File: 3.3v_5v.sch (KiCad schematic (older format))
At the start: 15 parts, among them J1 Jack-DC, SW1 SW_Push_SPDT, U1 AP1117-33

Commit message: duży update, gotowe pcb
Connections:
- net labels added: GNDA
- wire segments 27 -> 30
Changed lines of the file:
@@
 EESchema Schematic File Version 4
+LIBS:WELLER-cache
 EELAYER 29 0
 EELAYER END
@@
 $EndComp
 Wire Wire Line
-	3300 2650 3600 2650
+	3300 2650 3450 2650
 $Comp
 L power:GND #PWR0106
@@
 $EndComp
 Wire Wire Line
-	4000 3600 4000 2950
+	4000 3600 4000 3100
 Wire Wire Line
 	3600 2950 3600 3600
@@
 Wire Wire Line
 	2000 2550 2200 2550
+$Comp
+L power:PWR_FLAG #FLG0102
+U 1 1 5CF25261
+P 3450 2650
+F 0 "#FLG0102" H 3450 2725 50  0001 C CNN
+F 1 "PWR_FLAG" H 3450 2823 50  0000 C CNN
+F 2 "" H 3450 2650 50  0001 C CNN
+F 3 "~" H 3450 2650 50  0001 C CNN
+	1    3450 2650
+	1    0    0    -1
+$EndComp
+Connection ~ 3450 2650
+Wire Wire Line
+	3450 2650 3600 2650
+$Comp
+L power:PWR_FLAG #FLG0103
+U 1 1 5CF256F8
+P 4000 3100
+F 0 "#FLG0103" H 4000 3175 50  0001 C CNN
+F 1 "PWR_FLAG" V 4000 3228 50  0000 L CNN
+F 2 "" H 4000 3100 50  0001 C CNN
+F 3 "~" H 4000 3100 50  0001 C CNN
+	1    4000 3100
+	0    1    1    0
+$EndComp
+Connection ~ 4000 3100
+Wire Wire Line
+	4000 3100 4000 2950
+$Comp
+L power:GND #PWR0136
+U 1 1 5CEE3547
+P 4600 4350
+F 0 "#PWR0136" H 4600 4100 50  0001 C CNN
+F 1 "GND" H 4605 4177 50  0000 C CNN
+F 2 "" H 4600 4350 50  0001 C CNN
+F 3 "" H 4600 4350 50  0001 C CNN
+	1    4600 4350
+	1    0    0    -1
+$EndComp
+$Comp
+L power:GNDA #PWR0140
+U 1 1 5CEE3C79
+P 4850 4350
+F 0 "#PWR0140" H 4850 4100 50  0001 C CNN
+F 1 "GNDA" H 4855 4177 50  0000 C CNN
+F 2 "" H 4850 4350 50  0001 C CNN
+F 3 "" H 4850 4350 50  0001 C CNN
+	1    4850 4350
+	1    0    0    -1
+$EndComp
+Wire Wire Line
+	4600 4350 4850 4350
 $EndSCHEMATC

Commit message: duży update, drc przechodzi
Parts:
- removed H1, H2, H3, H4: MountingHole, MountingHole:MountingHole_2.2mm_M2, symbol Mechanical:MountingHole
- J1: footprint Connector_BarrelJack:BarrelJack_Horizontal -> symbols:jackDC_cutout
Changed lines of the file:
@@
 EESchema Schematic File Version 4
 LIBS:WELLER-cache
-EELAYER 26 0
+EELAYER 29 0
 EELAYER END
 $Descr A4 11693 8268
@@
 F 0 "J1" H 1057 3075 50  0000 C CNN
 F 1 "Jack-DC" H 1057 2984 50  0000 C CNN
-F 2 "Connector_BarrelJack:BarrelJack_Horizontal" H 1050 2710 50  0001 C CNN
+F 2 "symbols:jackDC_cutout" H 1050 2710 50  0001 C CNN
 F 3 "~" H 1050 2710 50  0001 C CNN
 	1    1000 2750
@@
 	2200 2550 2200 2650
 Connection ~ 2200 2650
-$Comp
-L Mechanical:MountingHole H1
-U 1 1 5CC1244A
-P 2950 1200
-F 0 "H1" H 3050 1246 50  0000 L CNN
-F 1 "MountingHole" H 3050 1155 50  0000 L CNN
-F 2 "MountingHole:MountingHole_2.2mm_M2" H 2950 1200 50  0001 C CNN
-F 3 "~" H 2950 1200 50  0001 C CNN
-	1    2950 1200
-	1    0    0    -1
-$EndComp
-$Comp
-L Mechanical:MountingHole H2
-U 1 1 5CC12623
-P 2950 1400
-F 0 "H2" H 3050 1446 50  0000 L CNN
-F 1 "MountingHole" H 3050 1355 50  0000 L CNN
-F 2 "MountingHole:MountingHole_2.2mm_M2" H 2950 1400 50  0001 C CNN
-F 3 "~" H 2950 1400 50  0001 C CNN
-	1    2950 1400
-	1    0    0    -1
-$EndComp
-$Comp
-L Mechanical:MountingHole H3
-U 1 1 5CC127F9
-P 2950 1600
-F 0 "H3" H 3050 1646 50  0000 L CNN
-F 1 "MountingHole" H 3050 1555 50  0000 L CNN
-F 2 "MountingHole:MountingHole_2.2mm_M2" H 2950 1600 50  0001 C CNN
-F 3 "~" H 2950 1600 50  0001 C CNN
-	1    2950 1600
-	1    0    0    -1
-$EndComp
-$Comp
-L Mechanical:MountingHole H4
-U 1 1 5CC129B7
-P 2950 1800
-F 0 "H4" H 3050 1846 50  0000 L CNN
-F 1 "MountingHole" H 3050 1755 50  0000 L CNN
-F 2 "MountingHole:MountingHole_2.2mm_M2" H 2950 1800 50  0001 C CNN
-F 3 "~" H 2950 1800 50  0001 C CNN
-	1    2950 1800
-	1    0    0    -1
-$EndComp
 Wire Wire Line
 	1550 2450 1550 2350

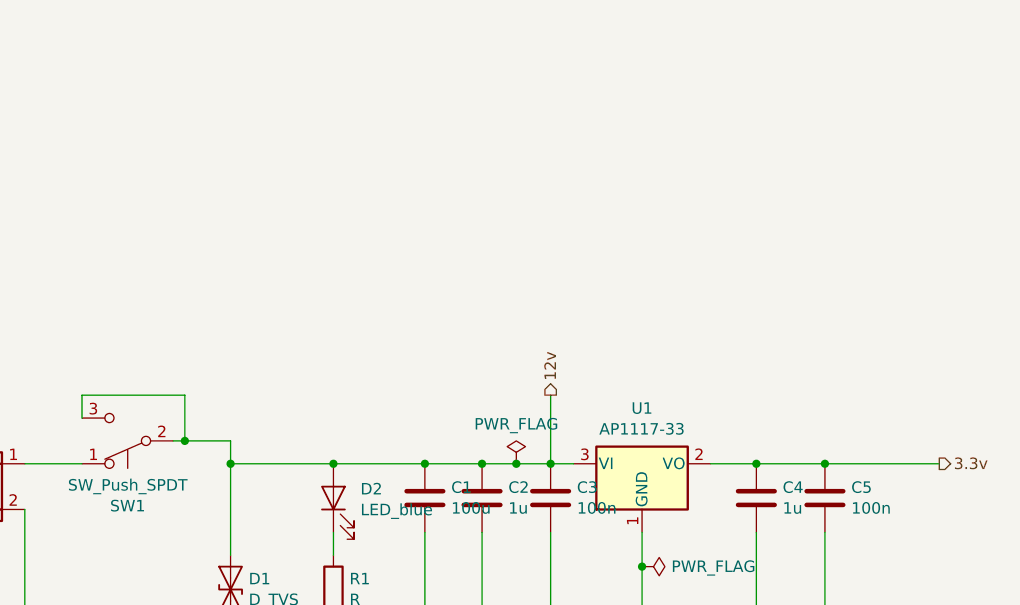
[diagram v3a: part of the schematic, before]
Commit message: dodanie pomiaru napięcia zasilającego grzałkę
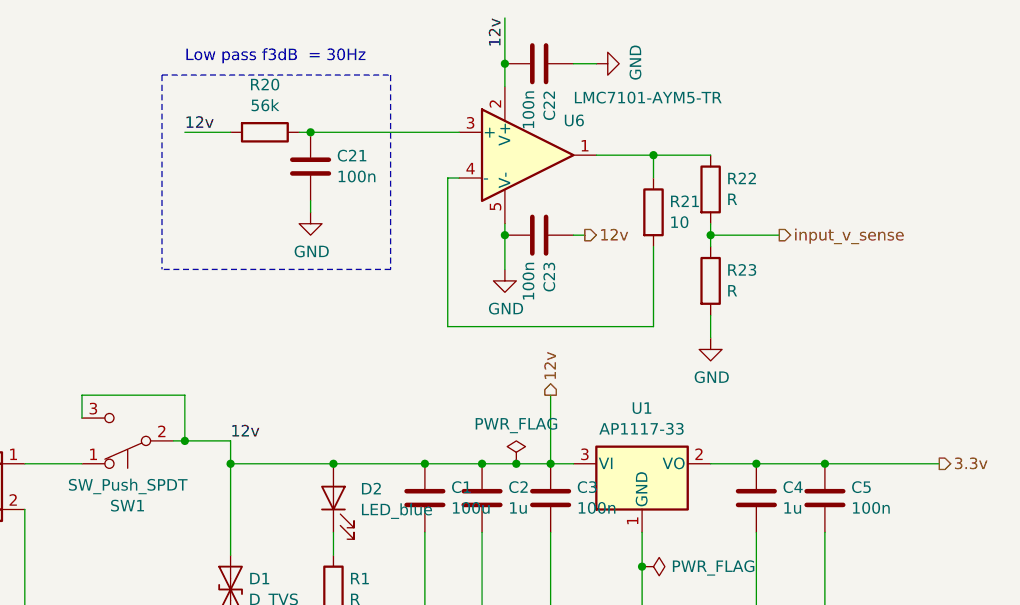
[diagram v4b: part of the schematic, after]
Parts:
- added C21, C22, C23: 100n, Capacitor_SMD:C_0603_1608Metric_Pad1.05x0.95mm_HandSolder, symbol Device:C
- added R20: 56k, Resistor_SMD:R_0603_1608Metric_Pad1.05x0.95mm_HandSolder, symbol Device:R
- added R21: 10, Resistor_SMD:R_0603_1608Metric_Pad1.05x0.95mm_HandSolder, symbol Device:R
- added R22, R23: R, Resistor_SMD:R_0603_1608Metric_Pad1.05x0.95mm_HandSolder, symbol Device:R
- added U6: LMC7101-AYM5-TR, Package_TO_SOT_SMD:SOT-23-5, symbol russian-nixies:LMC7101-AYM5-TR
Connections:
- net 12v: now also C22.2, C23.1, R20.2, U6.2 (V+)
- net GND: now also C21.2, C22.1, C23.2, R23.2, U6.5 (V-)
- new net: R21.1, R22.1, U6.1
- new net: C21.1, R20.1, U6.3 (+)
- new net: R21.2, U6.4 (-)
- new net input_v_sense: R22.2, R23.1
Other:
- note added: "Low pass f3dB = 30Hz"
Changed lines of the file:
@@
 Wire Wire Line
 	4600 4350 4850 4350
+$Comp
+L russian-nixies:LMC7101-AYM5-TR U6
+U 1 1 5D06EFCA
+P 3500 1300
+F 0 "U6" H 3750 1450 50  0000 R CNN
+F 1 "LMC7101-AYM5-TR" H 4350 1550 50  0000 R CNN
+F 2 "Package_TO_SOT_SMD:SOT-23-5" H 3400 1100 50  0001 L CNN
+F 3 "http://ww1.microchip.com/downloads/en/DeviceDoc/22141b.pdf" H 3500 1500 50  0001 C CNN
+	1    3500 1300
+	1    0    0    -1
+$EndComp
+$Comp
+L power:GND #PWR0132
+U 1 1 5D072379
+P 3400 1800
+F 0 "#PWR0132" H 3400 1550 50  0001 C CNN
+F 1 "GND" H 3405 1627 50  0000 C CNN
+F 2 "" H 3400 1800 50  0001 C CNN
+F 3 "" H 3400 1800 50  0001 C CNN
+	1    3400 1800
+	1    0    0    -1
+$EndComp
+$Comp
+L Device:C C23
+U 1 1 5D072847
+P 3550 1650
+F 0 "C23" H 3665 1696 50  0000 L CNN
+F 1 "100n" H 3665 1605 50  0000 L CNN
+F 2 "Capacitor_SMD:C_0603_1608Metric_Pad1.05x0.95mm_HandSolder" H 3588 1500 50  0001 C CNN
+F 3 "~" H 3550 1650 50  0001 C CNN
+	1    3550 1650
+	0    1    1    0
+$EndComp
+$Comp
+L Device:C C22
+U 1 1 5D072EC9
+P 3550 900
+F 0 "C22" H 3665 946 50  0000 L CNN
+F 1 "100n" H 3665 855 50  0000 L CNN
+F 2 "Capacitor_SMD:C_0603_1608Metric_Pad1.05x0.95mm_HandSolder" H 3588 750 50  0001 C CNN
+F 3 "~" H 3550 900 50  0001 C CNN
+	1    3550 900
+	0    1    1    0
+$EndComp
+Wire Wire Line
+	3400 1000 3400 900
+Connection ~ 3400 900
+Wire Wire Line
+	3400 900  3400 700
+Wire Wire Line
+	3400 1600 3400 1650
+Connection ~ 3400 1650
+Wire Wire Line
+	3400 1650 3400 1800
+$Comp
+L power:GND #PWR0133
+U 1 1 5D076440
+P 3800 900
+F 0 "#PWR0133" H 3800 650 50  0001 C CNN
+F 1 "GND" H 3805 727 50  0000 C CNN
+F 2 "" H 3800 900 50  0001 C CNN
+F 3 "" H 3800 900 50  0001 C CNN
+	1    3800 900
+	0    -1   -1   0
+$EndComp
+Wire Wire Line
+	3800 900  3700 900
+Text HLabel 3750 1650 2    50   Output ~ 0
+12v
+Wire Wire Line
+	3750 1650 3700 1650
+Wire Wire Line
+	3800 1300 4050 1300
+Text HLabel 4600 1650 2    50   Output ~ 0
+input_v_sense
+Wire Wire Line
+	3150 1400 3150 2050
+Wire Wire Line
+	3150 2050 4050 2050
+Wire Wire Line
+	4050 2050 4050 1700
+Wire Wire Line
+	3150 1400 3200 1400
+$Comp
+L Device:R R21
+U 1 1 5D079D81
+P 4050 1550
+F 0 "R21" H 4120 1596 50  0000 L CNN
+F 1 "10" H 4120 1505 50  0000 L CNN
+F 2 "Resistor_SMD:R_0603_1608Metric_Pad1.05x0.95mm_HandSolder" V 3980 1550 50  0001 C CNN
+F 3 "~" H 4050 1550 50  0001 C CNN
+	1    4050 1550
+	1    0    0    -1
+$EndComp
+Wire Wire Line
+	4050 1300 4050 1400
+Connection ~ 4050 1300
+Wire Wire Line
+	4050 1300 4300 1300
+$Comp
+L Device:R R20
+U 1 1 5D07C6AC
+P 2350 1200
+F 0 "R20" V 2143 1200 50  0000 C CNN
+F 1 "56k" V 2234 1200 50  0000 C CNN
+F 2 "Resistor_SMD:R_0603_1608Metric_Pad1.05x0.95mm_HandSolder" V 2280 1200 50  0001 C CNN
+F 3 "~" H 2350 1200 50  0001 C CNN
+	1    2350 1200
+	0    1    1    0
+$EndComp
+$Comp
+L Device:C C21
+U 1 1 5D07CF1C
+P 2550 1350
+F 0 "C21" H 2665 1396 50  0000 L CNN
+F 1 "100n" H 2665 1305 50  0000 L CNN
+F 2 "Capacitor_SMD:C_0603_1608Metric_Pad1.05x0.95mm_HandSolder" H 2588 1200 50  0001 C CNN
+F 3 "~" H 2550 1350 50  0001 C CNN
+	1    2550 1350
+	1    0    0    -1
+$EndComp
+$Comp
+L power:GND #PWR0135
+U 1 1 5D07D74D
+P 2550 1550
+F 0 "#PWR0135" H 2550 1300 50  0001 C CNN
+F 1 "GND" H 2555 1377 50  0000 C CNN
+F 2 "" H 2550 1550 50  0001 C CNN
+F 3 "" H 2550 1550 50  0001 C CNN
+	1    2550 1550
+	1    0    0    -1
+$EndComp
+Wire Wire Line
+	2550 1550 2550 1500
+Wire Wire Line
+	2500 1200 2550 1200
+Connection ~ 2550 1200
+Wire Wire Line
+	2550 1200 3200 1200
+Wire Wire Line
+	2000 1200 2200 1200
+Text Label 2200 2550 0    50   ~ 0
+12v
+Text Label 2000 1200 0    50   ~ 0
+12v
+Text Label 3400 700  3    50   ~ 0
+12v
+Text Notes 2000 900  0    50   ~ 0
+Low pass f3dB  = 30Hz
+Wire Notes Line
+	1900 950  2900 950
+Wire Notes Line
+	2900 1800 1900 1800
+Wire Notes Line
+	1900 950  1900 1800
+Wire Notes Line
+	2900 950  2900 1800
+$Comp
+L Device:R R22
+U 1 1 5D0A0AC8
+P 4300 1450
+F 0 "R22" H 4370 1496 50  0000 L CNN
+F 1 "R" H 4370 1405 50  0000 L CNN
+F 2 "Resistor_SMD:R_0603_1608Metric_Pad1.05x0.95mm_HandSolder" V 4230 1450 50  0001 C CNN
+F 3 "~" H 4300 1450 50  0001 C CNN
+	1    4300 1450
+	1    0    0    -1
+$EndComp
+$Comp
+L Device:R R23
+U 1 1 5D0A0DAA
+P 4300 1850
+F 0 "R23" H 4370 1896 50  0000 L CNN
+F 1 "R" H 4370 1805 50  0000 L CNN
+F 2 "Resistor_SMD:R_0603_1608Metric_Pad1.05x0.95mm_HandSolder" V 4230 1850 50  0001 C CNN
+F 3 "~" H 4300 1850 50  0001 C CNN
+	1    4300 1850
+	1    0    0    -1
+$EndComp
+$Comp
+L power:GND #PWR0141
+U 1 1 5D0A0FB3
+P 4300 2100
+F 0 "#PWR0141" H 4300 1850 50  0001 C CNN
+F 1 "GND" H 4305 1927 50  0000 C CNN
+F 2 "" H 4300 2100 50  0001 C CNN
+F 3 "" H 4300 2100 50  0001 C CNN
+	1    4300 2100
+	1    0    0    -1
+$EndComp
+Wire Wire Line
+	4300 2000 4300 2100
+Wire Wire Line
+	4300 1600 4300 1650
+Wire Wire Line
+	4600 1650 4300 1650
+Connection ~ 4300 1650
+Wire Wire Line
+	4300 1650 4300 1700
 $EndSCHEMATC

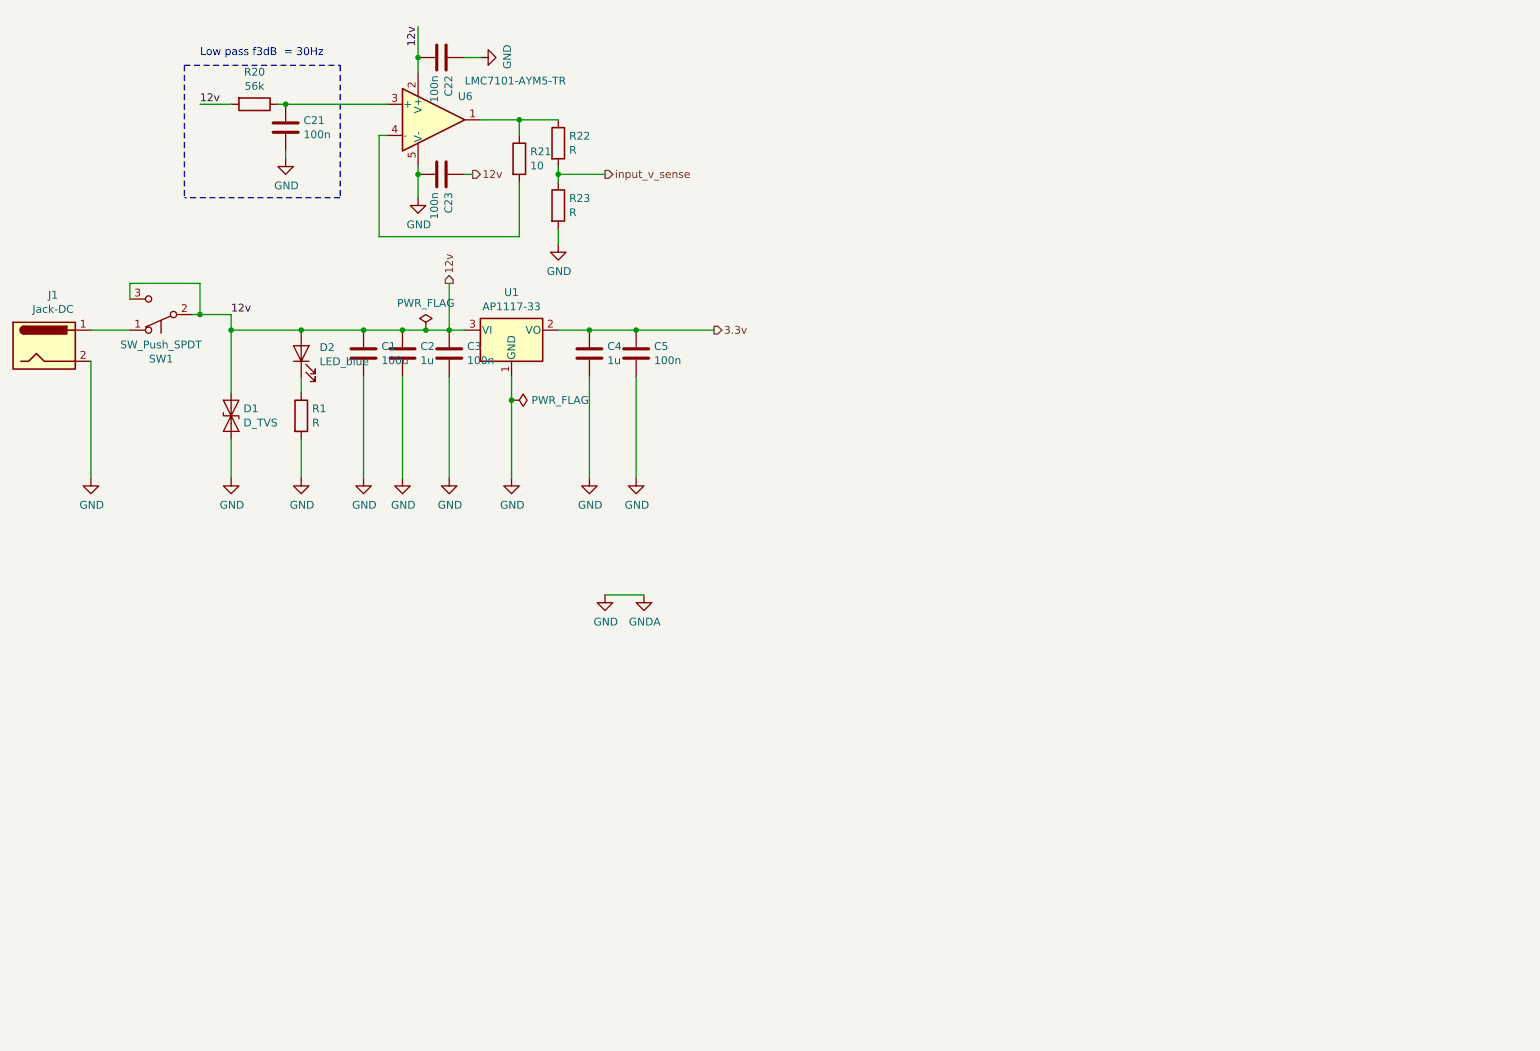
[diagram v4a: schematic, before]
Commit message: poprawki głownie na pcb zaokrąglenie strony z grotem
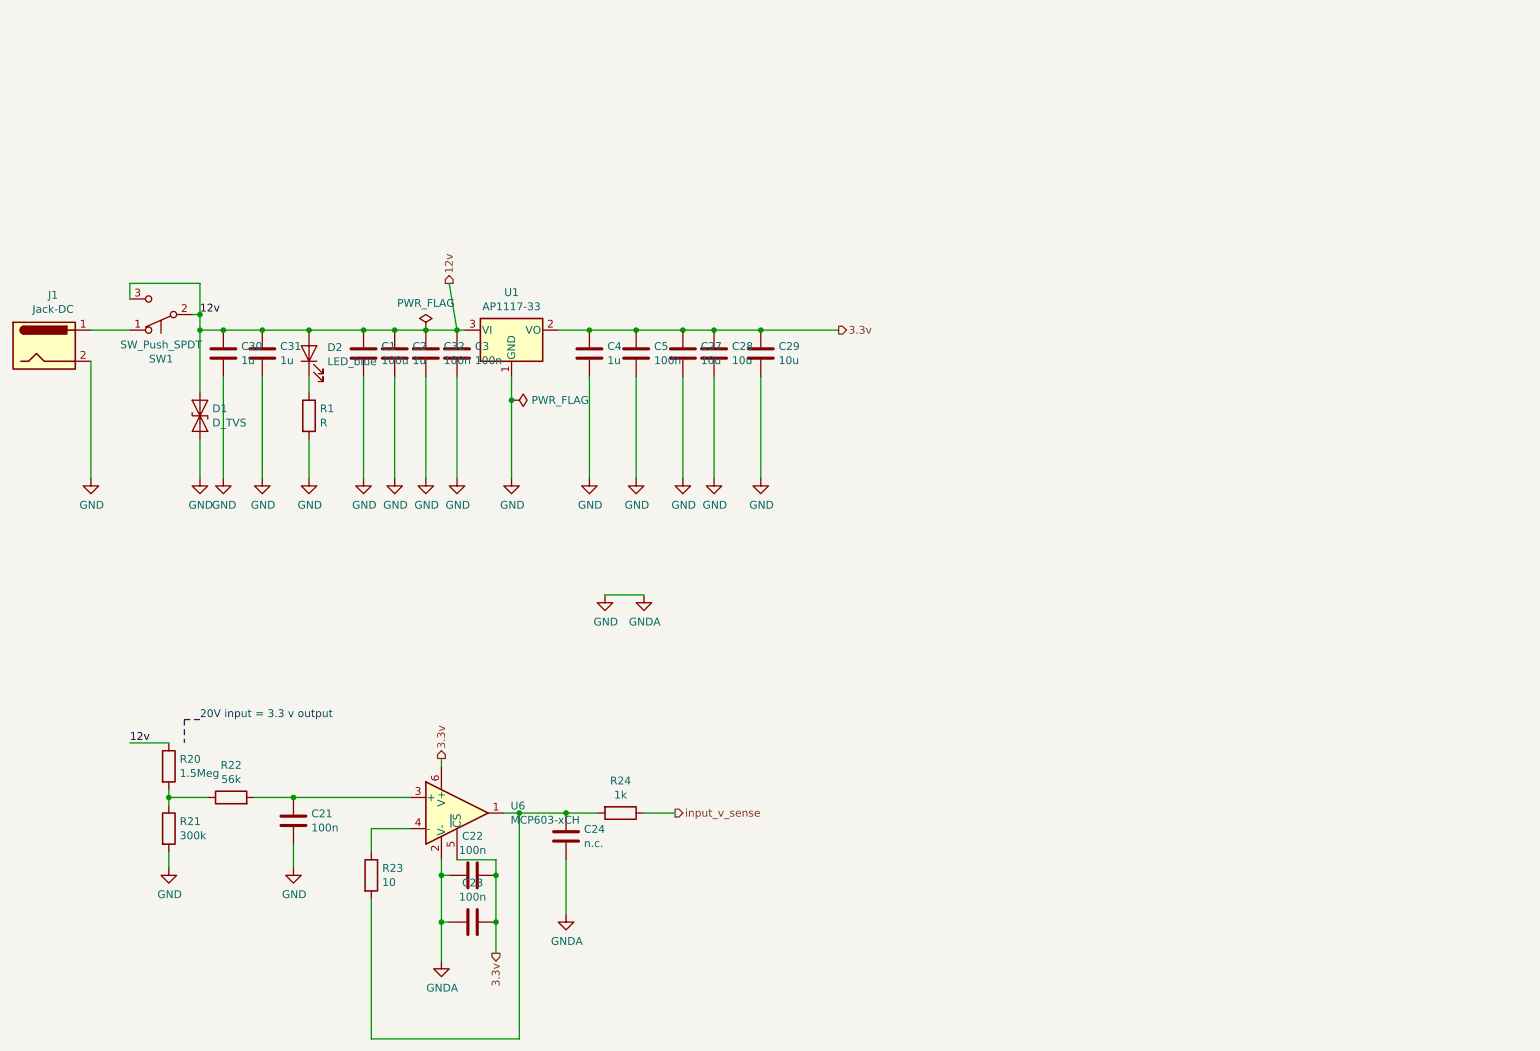
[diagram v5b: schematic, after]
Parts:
- removed U6: LMC7101-AYM5-TR, Package_TO_SOT_SMD:SOT-23-5, symbol russian-nixies:LMC7101-AYM5-TR
- added C24: n.c., Capacitor_SMD:C_0603_1608Metric, symbol Device:C
- added C27, C28, C29: 10u, Capacitor_SMD:C_0805_2012Metric, symbol Device:C
- added C30, C31: 1u, Capacitor_SMD:C_0805_2012Metric, symbol Device:C
- added C32: 100n, Capacitor_SMD:C_0603_1608Metric_Pad1.05x0.95mm_HandSolder, symbol Device:C
- added R24: 1k, Resistor_SMD:R_0603_1608Metric, symbol Device:R
- added U6: MCP603-xCH, Package_TO_SOT_SMD:SOT-23-6, symbol Amplifier_Operational:MCP603-xCH
- C23: footprint Capacitor_SMD:C_0603_1608Metric_Pad1.05x0.95mm_HandSolder -> Capacitor_SMD:C_0805_2012Metric
- R20: value 56k -> 1.5Meg
- R21: value 10 -> 300k
- R22: value R -> 56k; footprint Resistor_SMD:R_0603_1608Metric_Pad1.05x0.95mm_HandSolder -> Resistor_SMD:R_0603_1608Metric
- R23: value R -> 10; footprint Resistor_SMD:R_0603_1608Metric_Pad1.05x0.95mm_HandSolder -> Resistor_SMD:R_0603_1608Metric
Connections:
- net 12v: now also R20.1, C30.1, C31.1, C32.1; no longer C22.2, C23.1, R20.2
- net 3.3v: now also C22.2, C23.2, C27.1, C28.1, C29.1, U6.5 (~CS), U6.6 (V+)
- net GND: now also C23.1, R21.2, C24.2, C27.2, C28.2, C29.2, C30.2, C31.2, C32.2, U6.2 (V-); no longer C23.2, R23.2
- net input_v_sense: now also R24.1; no longer R22.2, R23.1
- net at R21.1, R22.1: now also R20.2
- net at C21.1: now also R22.2, U6.3 (+); no longer R20.1
- new net: C24.1, R23.2, R24.2, U6.1
- new net: R23.1, U6.4 (-)
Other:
- note added: "20V input = 3.3 v output"
- note removed: "Low pass f3dB = 30Hz"
- moved on the sheet: C2, C3, D1, D2, R1

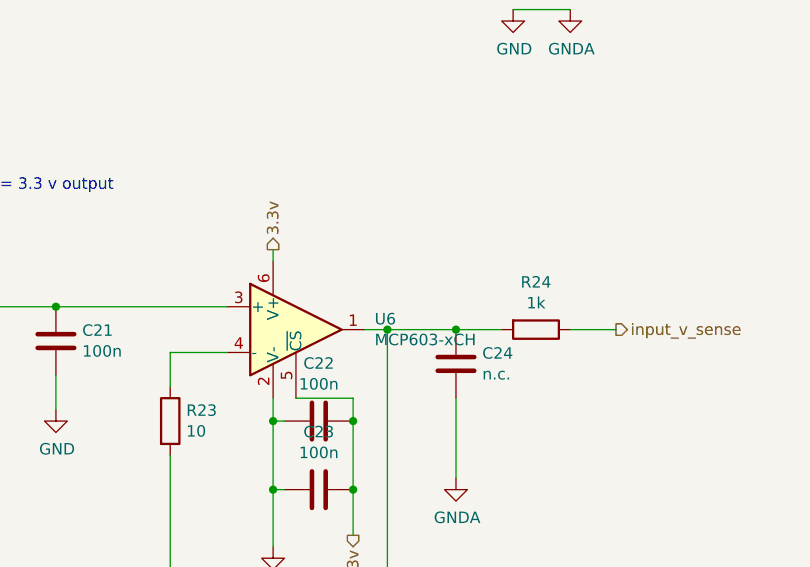
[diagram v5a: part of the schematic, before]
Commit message: wyciecie przy gnieździe jack - dodanie 3d gniazda, update jpg
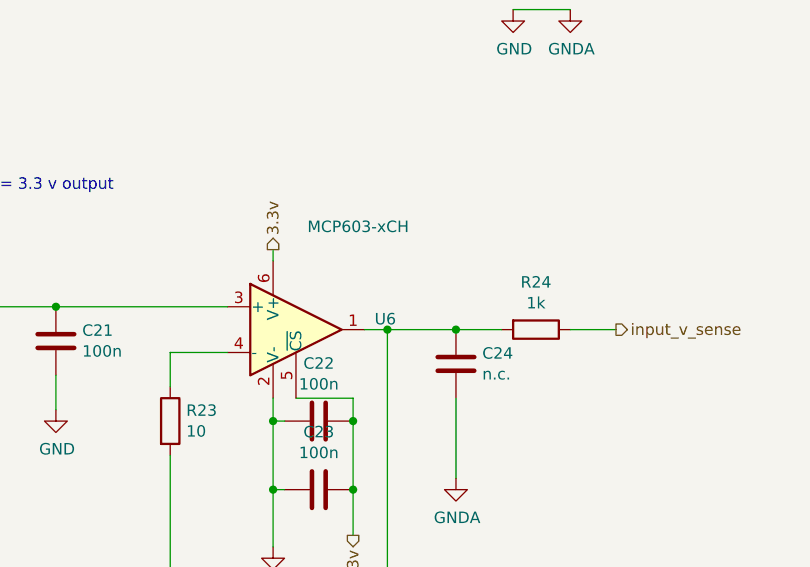
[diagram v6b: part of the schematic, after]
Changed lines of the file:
@@
 AR Path="/5CB5C0EA/5D0FCAD5" Ref="U6"  Part="1"
 F 0 "U6" H 3994 5796 50  0000 L CNN
-F 1 "MCP603-xCH" H 3994 5705 50  0000 L CNN
+F 1 "MCP603-xCH" H 3700 6200 50  0000 L CNN
 F 2 "Package_TO_SOT_SMD:SOT-23-6" H 3650 5750 50  0001 L CNN
 F 3 "https://www.tme.eu/Document/718e1e465ad4ed1ffbd9a510b0eda58e/mcp6031.pdf" H 3700 5950 50  0001 C CNN
